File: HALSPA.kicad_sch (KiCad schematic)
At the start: 7 parts, among them J1 Conn_02x04_Odd_Even, J2 Conn_02x02_Odd_Even, J3 Conn_02x04_Odd_Even, J4 Conn_02x02_Odd_Even, J5 Conn_02x02_Odd_Even

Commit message: WIP v0.2.0 changes
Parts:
- added J50: Conn_01x08, HL_Connector_Pad_2.54mm:Pad_1x08_P2.54_1.7x1.7_Rect-Rnd, symbol Connector_Generic:Conn_01x08
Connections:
- net GND: now also J50.1 (Pin_1)
- new net AAL1: J50.7 (Pin_7)
- new net AAL2: J50.8 (Pin_8)
- new net UEN: J50.3 (Pin_3)
- new net ~{DINT1}: J50.6 (Pin_6)
- new net ~{DINT2}: J50.5 (Pin_5)
- new net ~{PINT}: J50.2 (Pin_2)
- new net ~{UFLT}: J50.4 (Pin_4)
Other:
- removed sheet Filters
- sheet ADC ports: added ALERT1, ALERT2; removed none
- sheet DUT Power ports: added ~{INT}; removed none
- sheet Digital IO ports: added ~{INT1}, ~{INT2}; removed none
- sheet MCU 2: file mcu.kicad_sch -> mcu2.kicad_sch
- sheet USB connector ports: added EN, ~{FAULT}; removed none

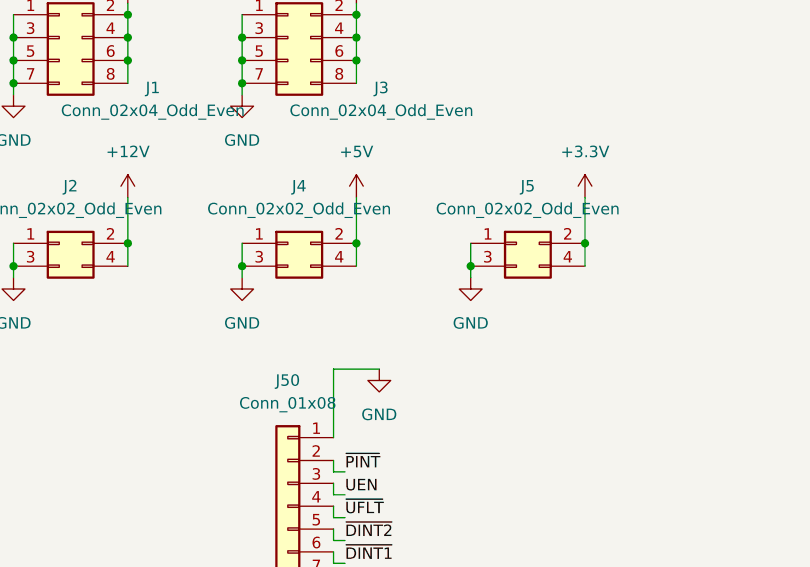
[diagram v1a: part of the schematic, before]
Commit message: Assign part numbers and finish other 0.2.0 changes
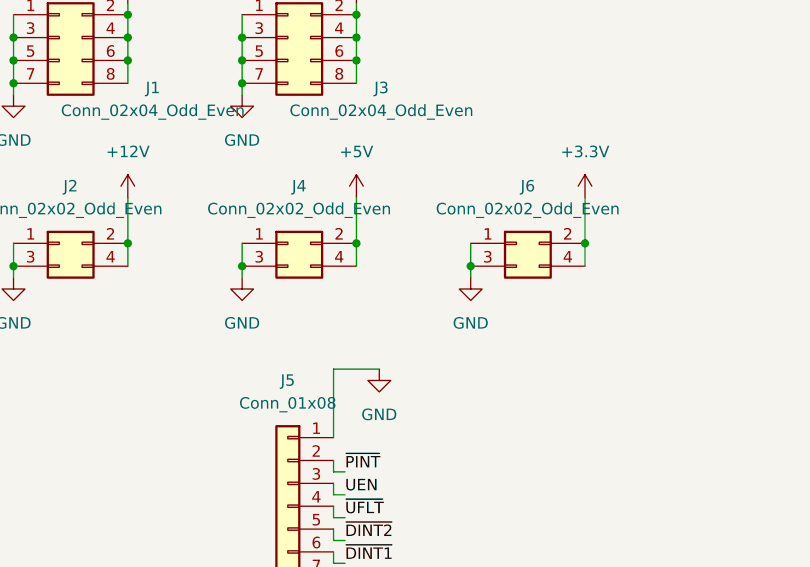
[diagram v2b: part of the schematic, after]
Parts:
- J1, J3: LCSC (none) -> C7501275
- J5: renamed from J50; LCSC (none) -> C492407
- renumbered J5 to J6
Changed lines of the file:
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@@
 		(dnp no)
 		(fields_autoplaced yes)
-		(property "Reference" "#PWR013"
+		(property "Reference" "#PWR014"
 			(at 77.47 95.25 0)
 			(effects
@@
 			(project "HALSPA"
 				(path "/7eeba806-440e-4671-bc07-69fe183910a7"
-					(reference "#PWR013")
+					(reference "#PWR014")
 					(unit 1)
 				)
@@
 			)
 		)
+		(property "LCSC" "C7501275"
+			(at 31.75 62.23 0)
+			(effects
+				(font
+					(size 1.27 1.27)
+				)
+				(hide yes)
+			)
+		)
 		(pin "3"
 		)
@@
 		(dnp no)
 		(fields_autoplaced yes)
-		(property "Reference" "J5"
+		(property "Reference" "J6"
 			(at 83.82 78.74 0)
 			(effects
@@
 			(project "HALSPA"
 				(path "/7eeba806-440e-4671-bc07-69fe183910a7"
-					(reference "J5")
+					(reference "J6")
 					(unit 1)
 				)
@@
 		(dnp no)
 		(fields_autoplaced yes)
-		(property "Reference" "#PWR014"
+		(property "Reference" "#PWR015"
 			(at 90.17 83.82 0)
 			(effects
@@
 			(project "HALSPA"
 				(path "/7eeba806-440e-4671-bc07-69fe183910a7"
-					(reference "#PWR014")
+					(reference "#PWR015")
 					(unit 1)
 				)
@@
 		(dnp no)
 		(fields_autoplaced yes)
-		(property "Reference" "J50"
+		(property "Reference" "J5"
 			(at 57.15 100.33 0)
 			(effects
@@
 			)
 		)
+		(property "LCSC" "C492407"
+			(at 57.15 114.3 0)
+			(effects
+				(font
+					(size 1.27 1.27)
+				)
+				(hide yes)
+			)
+		)
 		(pin "4"
 		)
@@
 			(project ""
 				(path "/7eeba806-440e-4671-bc07-69fe183910a7"
-					(reference "J50")
+					(reference "J5")
 					(unit 1)
 				)
@@
 		(dnp no)
 		(fields_autoplaced yes)
-		(property "Reference" "#PWR0218"
+		(property "Reference" "#PWR013"
 			(at 67.31 105.41 0)
 			(effects
@@
 			(project "HALSPA"
 				(path "/7eeba806-440e-4671-bc07-69fe183910a7"
-					(reference "#PWR0218")
+					(reference "#PWR013")
 					(unit 1)
 				)
@@
 			)
 		)
+		(property "LCSC" "C7501275"
+			(at 57.15 62.23 0)
+			(effects
+				(font
+					(size 1.27 1.27)
+				)
+				(hide yes)
+			)
+		)

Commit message: Update the title blocks
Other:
- company: (none) -> Hat Labs Oy
- title: (none) -> HALSPA - Hat Labs Spaghetti Board
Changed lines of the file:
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@@
 	(generator_version "9.0")
 	(paper "A4")
+	(title_block
+		(title "HALSPA - Hat Labs Spaghetti Board")
+		(date "2025-04-17")
+		(rev "v0.2.0")
+		(company "Hat Labs Oy")
+		(comment 1 "See the accompanying LICENSE.md file for license details.")
+	)
 	(junction
 		(at 26.67 62.23)

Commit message: Add JLCPCB corrections
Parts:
- J1, J3: JLCPCB_CORRECTION (none) -> 1.27;3.81;270
- J2, J4, J6: JLCPCB_CORRECTION (none) -> 1.27;1.27;270
- J5: JLCPCB_CORRECTION (none) -> 0;8.89;270
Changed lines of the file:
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@@
+			)
+		)
+		(property "JLCPCB_CORRECTION" "1.27;3.81;270"
+			(at 31.75 62.23 0)
+			(effects
+				(font
+					(size 1.27 1.27)
+				)
+				(hide yes)
 			)
 		)
@@
 			)
 		)
+		(property "JLCPCB_CORRECTION" "1.27;1.27;270"
+			(at 57.15 85.09 0)
+			(effects
+				(font
+					(size 1.27 1.27)
+				)
+				(hide yes)
+			)
+		)
 		(pin "1"
 		)
@@
 			)
 		)
+		(property "JLCPCB_CORRECTION" "1.27;1.27;270"
+			(at 82.55 85.09 0)
+			(effects
+				(font
+					(size 1.27 1.27)
+				)
+				(hide yes)
+			)
+		)
 		(pin "1"
 		)
@@
 			)
 		)
+		(property "JLCPCB_CORRECTION" "0;8.89;270"
+			(at 57.15 114.3 0)
+			(effects
+				(font
+					(size 1.27 1.27)
+				)
+				(hide yes)
+			)
+		)
 		(pin "4"
 		)
@@
 			)
 		)
+		(property "JLCPCB_CORRECTION" "1.27;1.27;270"
+			(at 31.75 85.09 0)
+			(effects
+				(font
+					(size 1.27 1.27)
+				)
+				(hide yes)
+			)
+		)
 		(pin "1"
 		)
@@
 			(at 57.15 62.23 0)
 			(effects
+				(font
+					(size 1.27 1.27)
+				)
+				(hide yes)
+			)
+		)
+		(property "JLCPCB_CORRECTION" "1.27;3.81;270"
+			(at 57.15 62.23 0)
+			(effects

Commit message: Assorted fixes
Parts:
- added J106, J107: Conn_02x02_Odd_Even, HL_Connector_Pad_2.54mm:Pad_2x02_P2.54_1.7x1.7_Rect-Rnd, symbol Connector_Generic:Conn_02x02_Odd_Even
- added J127, J128, J129, J130, J131, J132, J133, J134, J135: Conn_01x03, HL_Connector_Pad_2.54mm:Pad_1x03_P2.54_1.7x1.7_Rect-2Rnd, symbol Connector_Generic:Conn_01x03
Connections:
- net +3.3V: now also J107.2 (Pin_2), J107.4 (Pin_4), J127.3 (Pin_3), J128.3 (Pin_3), J129.3 (Pin_3), J130.3 (Pin_3), J131.3 (Pin_3), J132.3 (Pin_3), J133.3 (Pin_3), J134.3 (Pin_3), J135.3 (Pin_3)
- net +5V: now also J106.2 (Pin_2), J106.4 (Pin_4), J127.2 (Pin_2), J128.2 (Pin_2), J129.2 (Pin_2), J130.2 (Pin_2), J131.2 (Pin_2), J132.2 (Pin_2), J133.2 (Pin_2), J134.2 (Pin_2), J135.2 (Pin_2)
- net GND: now also J106.1 (Pin_1), J106.3 (Pin_3), J107.1 (Pin_1), J107.3 (Pin_3), J127.1 (Pin_1), J128.1 (Pin_1), J129.1 (Pin_1), J130.1 (Pin_1), J131.1 (Pin_1), J132.1 (Pin_1), J133.1 (Pin_1), J134.1 (Pin_1), J135.1 (Pin_1)
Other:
- moved on the sheet: J4, J5, J6
